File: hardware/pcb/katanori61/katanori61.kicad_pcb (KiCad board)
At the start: 2 copper layers, 82 x 37.4 mm, 59 parts, among them J1 XIAO RISER, J10 BAT (JST-PH), J13 USB-C, J2 OLED, J4 SPK IN, J5 SPK OUT, J6 BTN2, J7 REED+TOGGLE, K31 G6S-2F DC5, Q1 MMUN2133LT1G, Q2 AO3401A, Q31 SS8050, U1 TPS61090RSAR, U2 MCP73871-2CCI/ML, U3 INA226AIDGSR, U4 AS5600-ASOM

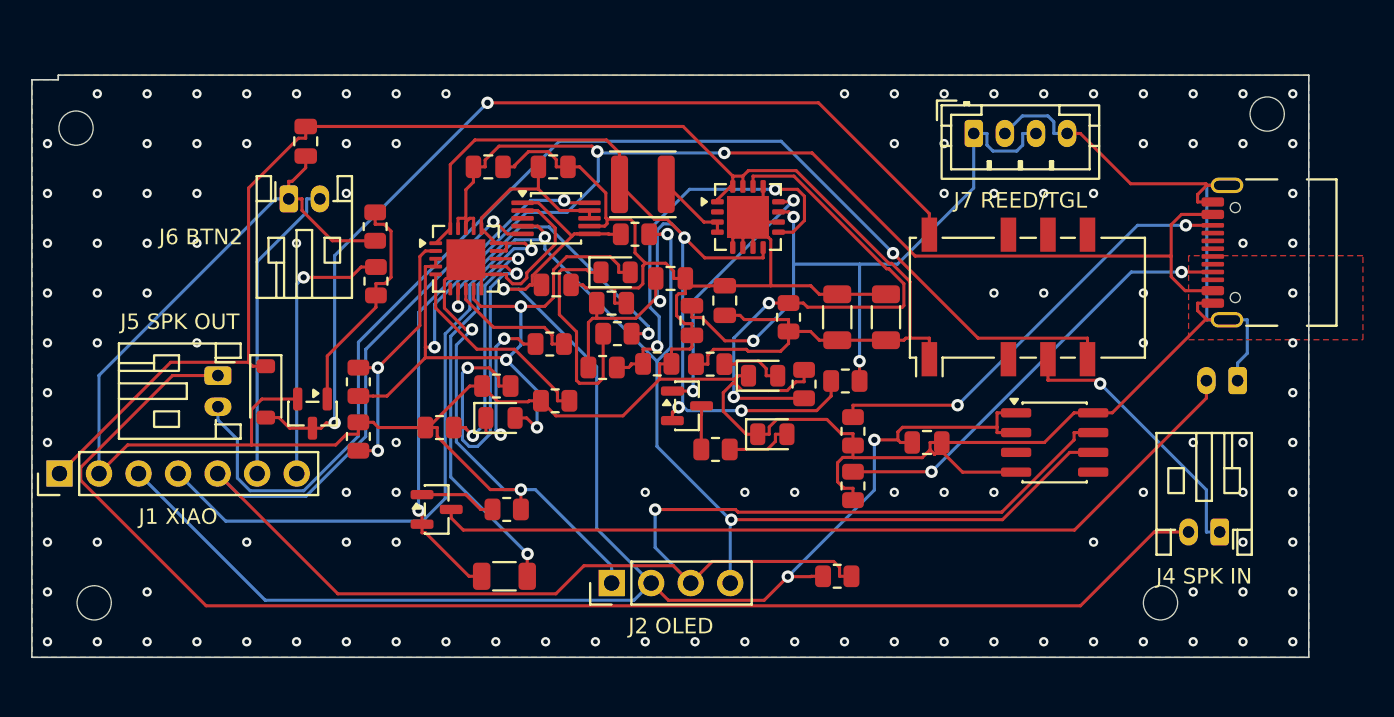
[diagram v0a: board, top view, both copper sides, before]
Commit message: pcb v6.1: J4 と J6 を縦の B2B-PH-K へ・J10 の極性を「手前が ＋ ・奥が GND」に戻す
🔒 ユーザー 2026-09-16 夕「J4とJ6を縦にして、J10の極性も手前奥に戻して」。

■ なぜ縦にしたか
J4（SPK IN）と J6（BTN2）は横出しで、抜く向きが**盤面の内側**（J4 は +Y・J6 は −Y）だった。
挿したプラグの胴が板の上へ 2.0 出るので、J4 は板の Y 14.30〜16.30、J6 は Y 21.20〜22.70 を塞ぐ。
gen_pcb の警告でも J4 の指の所に J13、J6 の指の所に R6・R7・D31・Q31・J1（背 8.5）が居て、
さらに「J6 の通り道が電池の下（挿し直すには電池を外す）」が出ていた。縦にすると全部消える。
筐体側は 56 個の模型でも plugpath が空で、殻は邪魔していない（別セッションが確認済み）。

■ J10 の極性が戻った
J10 のパッドを X 並びにしていたのは、J4 に挿さったプラグ（Y 14.30〜16.30）と
USB-C のシェルの足（20.63〜）に挟まれて 4.33 しか無く、6.9 の枠が入らなかったため。
J4 が縦になってその帯が消えたので **Y 並びへ戻した**。
  1 番 GND  → 板 (75.700, 16.950) ＝ 奥（ハッチ側）
  2 番 VBAT ＋ → 板 (75.700, 14.950) ＝ 手前（OLED 側）
PowerBoost B1 と同じ言い方に戻ったので、2026-09-16 夕に「左／右」で書き直した手順は
もう一度「手前／奥」に戻る。docs/PCB-V61.md 8 章を直した。

■ 置き直した枠（板の座標）
  J4  X 71.850〜78.750 / Y  6.250〜11.750（旧 Y 6.20〜14.80）。パッドは Y 8.45
      ⚠ 芯の Y は 9.00。8.60 だと枠の前端が取付穴 (72.5, 3.5) のナット（半径 2.56）へ 0.21 入る
  J6  X 14.050〜20.950 / Y 27.250〜32.750（旧 Y 22.70〜31.30）
  J10 X 73.500〜79.000 / Y 12.500〜19.400（旧 X 73.00〜79.90 / Y 14.475〜19.975）
      足は J4 の胴（Y 〜11.75）から 2.6・枠は USB-C の足（20.63）から 1.23

■ 足形は回路図が持っている
gen_pcb.py の BOX_PLACE だけ替えても足形は変わらない（place_footprint はネットリストの fp を使う）。
gen_sch.py の FP_PORT["PHIN"] と J6 の part() も B2B-PH-K へ替えること。
SPK OUT（J5）は口が板の**左の縁**（−X）を向いていて盤面を食わないので横出しのまま。
板の面に沿ってプラグが入るのは J5 だけになったので、gen_pcb の CONN も J5 だけにした。

■ 検査
回路図 0 件 / パッドの位置 11 点一致 / 重なり 0 / プラグの通り道 1 口すべて空き
DRC エラー 0・未接続 0・回路図との食い違い 0 / 銅箔のすきま 下回り 0 件（最小 0.151）
check_fab「奥（Y 16.95）が GND ／ 手前（Y 14.95）が VBAT」/ 地図の重なり なし
筐体 16 項目すべて期待値（hit_wires は 2.75 → 2.74）
STL 7 点 preflight: 中身 1 個・二重面 0・**🔴 0**（蓋の 0.22mm は 9072479 で解消済み）

■ 筐体側
pcb/v61_parts.scad を作り直した（gen_case_parts.py の PORTS も J4・J6 を上向きへ）。
SPK IN の線は「横から寄せて上から降ろす」形に引き直し。走る高さを
「嵌合したプラグの頭の 2.0 上」にした（旧 zl は横出しの背 4.8 を足した数で、縦の胴 6.0 ＋ 嵌合 2.0 より低く、プラグの頭を貫く）。
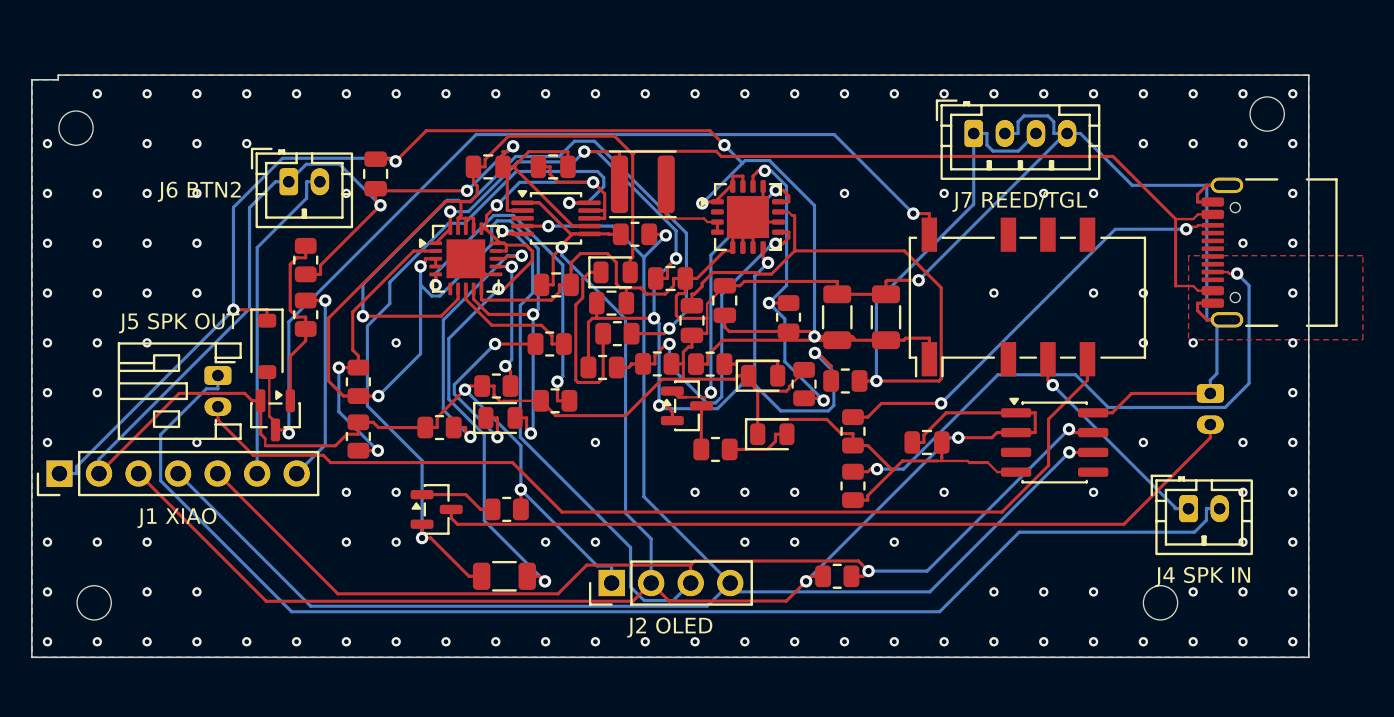
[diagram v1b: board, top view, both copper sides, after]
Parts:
- J4, J6: footprint Connector_JST:JST_PH_S2B-PH-K_1x02_P2.00mm_Horizontal -> Connector_JST:JST_PH_B2B-PH-K_1x02_P2.00mm_Vertical
- moved R31 5.00 mm to (57.6, 55.4)
- moved C31 4.96 mm to (62.1, 46.4)
- moved R32 4.95 mm to (57.6, 51.9)
- moved D31 2.93 mm to (55.1, 57.4)
- moved J4 2.50 mm to (114.3, 67.8), turned to 0 degrees
- moved Q31 2.38 mm to (55.6, 61.9)
- moved J10 1.93 mm to (115.7, 60.5), turned to 270 degrees
- moved J6 1.10 mm to (56.5, 46.9)
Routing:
- net STAT2: track 20.3 -> 45.5 mm
- net PROG3: track 23.6 -> 8.98 mm
- net SPKO: track 79.5 -> 65.8 mm, vias 1 -> 0
- net SCL: track 113.8 -> 100.2 mm, vias 2 -> 3
- net FB: track 35.0 -> 21.6 mm, vias 2 -> 3
- net BATP: track 33.3 -> 45.6 mm
- net EN: track 45.9 -> 57.5 mm, vias 3 -> 1
- net CC1: track 28.4 -> 38.5 mm
- net VBUS: track 125.7 -> 134.6 mm, vias 6 -> 4
- net THERM: track 13.5 -> 22.1 mm, vias 0 -> 2
- net VLIPO: track 41.8 -> 50.1 mm, vias 2 -> 4
- net V5: track 106.3 -> 113.8 mm, vias 0 -> 5
- net VSYS: track 71.9 -> 77.3 mm, vias 4 -> 7
- net SPKM: track 88.6 -> 83.4 mm
- net IN: track 17.7 -> 13.1 mm
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
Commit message: pcb v6.1: 前右の留め穴を外へ（板の X 72.5 → 79.354）。筐体 97fdee3 への追従
🔒 ユーザー「組む順で問題にならないのなら外側に出せるでしょ？」。筐体側が前右の柱を
世界 (74.5, 17) → (81.354, 17) へ出したので、板の穴も合わせる。

取付穴 4 点（板の座標）:
  左前 (4.0, 3.5)          左後ろ (2.834, 33.9942)
  右前 (79.354, 3.5) ←変更  右後ろ (79.354, 34.9)
右は前後とも X 79.354 でそろった。72.5 は「φ7 の柱の外周 78.0 が箱の隅の柱 78.354 まで 0.35」で
決まった数字で、後ろ 2 点を柱の芯へ出した e3a7162 のときに前右だけ内側に残っていた。

■ 検査
gen_pcb: パッドの位置 11 点一致・重なり 0・ナットの下に部品なし・パッドと穴のすきま 0.3 以上
DRC エラー 0・未接続 0・回路図との食い違い 0（自動配線は 1 回で 0 本残し）
check_pcb: 下回り 0 件（最小 0.151 = BATP ↔ VLIPO）
check_fab: 合わない所なし。取付穴 4 点とも φ2.20 を確認
地図の重なり なし

■ 筐体へ渡す物も作り直した
  v61_parts.scad   … 差分なし（穴は PCB_PARTS に入らない。部品も動いていない）
  v61_board3d.stl  … 板のメッシュ（穴が動いたので変わる）
  v61_parts3d.stl  … 差分なし
筐体の当たり検査 16 項目は穴を動かす前と全部同じ値で、STL 7 点も
中身 1 個・二重面 0・🔴 0 のまま（形は不変）。

⚠ 筐体側の指摘の記録: 「外へ出すと PH2（J4・J10）に当たる」は平面だけを見た誤りだった。
   柱は床から板の裏（Z 0〜12.0）、PH2 は板の上。Z では当たらない。
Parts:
- moved ? 6.85 mm to (119.4, 73.9)
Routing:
- net GND: vias 135 -> 136
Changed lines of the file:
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@@
 	(footprint "MountingHole:MountingHole_2.2mm_M2"
 		(layer "F.Cu")
-		(at 112.500 73.900)
+		(at 119.354 73.900)
 		(attr exclude_from_bom)
 		(pad "" np_thru_hole circle
@@
 	(segment
 		(start 66.9375 68.4517)
-		(end 67.3394 68.8536)
+		(end 67.3919 68.9061)
 		(width 0.200)
 		(layer "F.Cu")
@@
 	)
 	(segment
-		(start 67.3394 68.8536)
-		(end 110.1481 68.8536)
+		(start 67.3919 68.9061)
+		(end 110.0956 68.9061)
 		(width 0.200)
 		(layer "F.Cu")
@@
 	)
 	(segment
-		(start 110.1481 68.8536)
+		(start 110.0956 68.9061)
 		(end 115.7000 63.3017)
 		(width 0.200)
@@
 	(segment
 		(start 48.2681 66.0546)
-		(end 56.6872 74.4737)
+		(end 56.7364 74.5229)
 		(width 0.200)
 		(layer "B.Cu")
@@
 	)
 	(segment
-		(start 56.6872 74.4737)
-		(end 98.3110 74.4737)
+		(start 56.7364 74.5229)
+		(end 109.5206 74.5229)
 		(width 0.200)
 		(layer "B.Cu")
@@
 	)
 	(segment
-		(start 98.3110 74.4737)
-		(end 103.4220 69.3627)
-		(width 0.200)
-		(layer "B.Cu")
-		(net 24)
-	)
-	(segment
-		(start 103.4220 69.3627)
-		(end 114.6808 69.3627)
-		(width 0.200)
-		(layer "B.Cu")
-		(net 24)
-	)
-	(segment
-		(start 114.6808 69.3627)
+		(start 109.5206 74.5229)
 		(end 115.4483 68.5952)
 		(width 0.200)
@@
 	)
 	(via
+		(at 105.0000 70.0000)
+		(size 0.6)
+		(drill 0.3)
+		(layers "F.Cu" "B.Cu")
+		(net 11)
+	)
+	(via
 		(at 105.0000 47.6000)
 		(size 0.6)
@@
 	)
 	(via
+		(at 108.2000 70.0000)
+		(size 0.6)
+		(drill 0.3)
+		(layers "F.Cu" "B.Cu")
+		(net 11)
+	)
+	(via
 		(at 108.2000 66.8000)
 		(size 0.6)
@@
 	)
 	(via
+		(at 111.4000 70.0000)
+		(size 0.6)
+		(drill 0.3)
+		(layers "F.Cu" "B.Cu")
+		(net 11)
+	)
+	(via
 		(at 111.4000 63.6000)
 		(size 0.6)
@@
 	)
 	(via
-		(at 117.8000 73.2000)
-		(size 0.6)
-		(drill 0.3)
-		(layers "F.Cu" "B.Cu")
-		(net 11)
-	)
-	(via
 		(at 117.8000 70.0000)
 		(size 0.6)
@@
 		(size 0.6)
 		(drill 0.3)
-		(layers "F.Cu" "B.Cu")
-		(net 11)
-	)
-	(via
-		(at 121.0000 73.2000)
-		(size 0.6)
-		(drill 0.3)

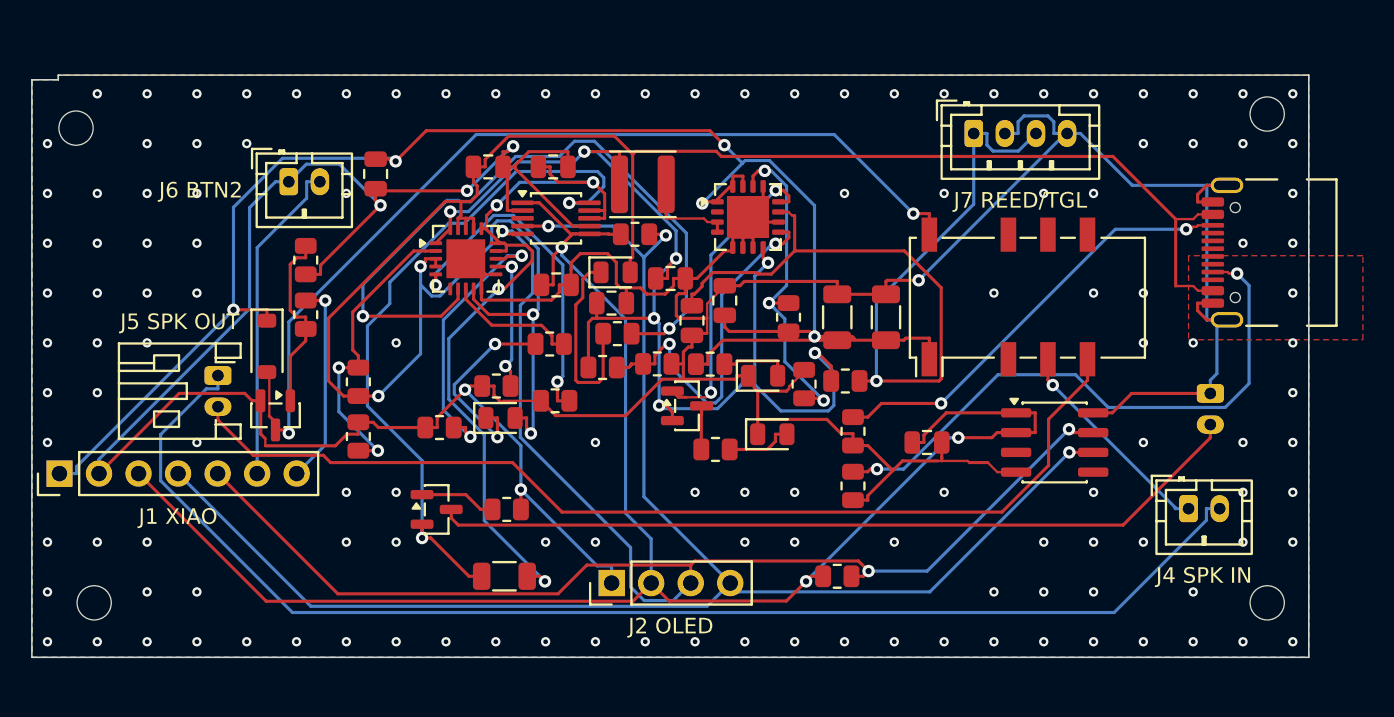
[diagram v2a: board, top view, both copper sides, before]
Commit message: pcb v6.1: 電源部を電流の順に並べ直す（電池の道 217 → 11.4 mΩ・INA226 のケルビン成立）
電源部は旧 PowerBoost 基板 → v6 → v6.1 の**二重の写し**で置かれていて、
v6.1 の板の上で並べた人がいなかった（gen_pcb.py の写しの注「ここで並べ直して
はいない」のまま）。その結果:

  ・電池の口 J10（板 X 76）からシャント R41（X 30）まで電流が板を横断し、
    自動配線の既定 0.2mm のままで配線 107mm ＝ 217mΩ
  ・シャント R41 と電流計 U3 が 23mm 離れ、センス線が R41 のパッドではなく
    11.9mΩ 手前（Q2 の足元）と 73.7mΩ 先（U2 の VBAT）から出ていた。
    INA226 は 10mΩ ではなく 96.7mΩ ＝ **9.7 倍**を見ていた
  ・USB-C J13 から充電 IC U2 まで 52mm

v5 で正しく読めていたのは、INA226 モジュールの上でシャントと IC が数 mm しか
離れておらず、ケルビンがモジュールの中で取れていたからである。v6.1 でシャントを
板に降ろしたときに、回路図（同じネット）は写ったが置き方（同じ点）が写らなかった。

並べ直し（板の座標で明示・写しをやめた）:
  J10 電池 → Q2 逆接保護 → R41 シャント → U2 充電 → L1・U1 昇圧 → J1 XIAO
  U3 は R41 の真上。USB-C は U2 のすぐ前の縁へ。

  電池の道      107mm 217.2mΩ → 13.7mm 11.4mΩ（充電 560mA で 6.4mV・1A で 11.4mV）
  R41 → U3      23.2mm → 3.0mm
  J13 → U2      52.0mm → 12.9mm
  ホットループ  7.4mm → 3.3mm（U1 を 180° 回して SW を L1 の側へ）
  SW            6.2mm → 4.6mm

入れた仕組み:
  ・dsn.py    ネットの組ごとの線幅（電池 0.6 / VSYS・SW・V5 0.4 / VBUS 0.2）
  ・gen_pcb.py PRE_TRACKS … 先に手で引いて固定する線。R41 のケルビン 2 本。
               ep_vias()  … U1・U2 の放熱パッドに GND ビア 4 本ずつ（配置から計算）
  ・route.py  locked の線と穴を merge で残し、SES に返る protect の写しは捨てる
  ・gen_sch.py R41 に「ケルビン必須・PRE_TRACKS を見よ」と経緯ごと残した

ついでに直したもの:
  ・USB-C を動かしたのに VBUS のベタが板の右端に残っていた（isolated_copper）。
    口の向きに追従させた
  ・Freerouting の最適化の段が、配線の段より悪い版から始めて書き出す（未接続 1 → 6）。
    統合基板で 2026-09-15 に見たのと同じ不具合。v6.1 側でも切った

検算: 未接続 0 ／ 回路図との差 0 ／ DRC エラー 0 ／ 銅のすきま 下回り 0。
ケルビンは「負荷の道 ＋ センス線 ＝ 直に測った値」の一致で成立を確認した。

残る警告: silk_over_copper 2 件（U1・U2 のシルクの角が隣のパッドに 0.1 乗る。
逃がすと未接続が 2 本出たので警告を取った）。lib_footprint_issues 59 件と
silk_edge_clearance 2 件は以前からあるもの。
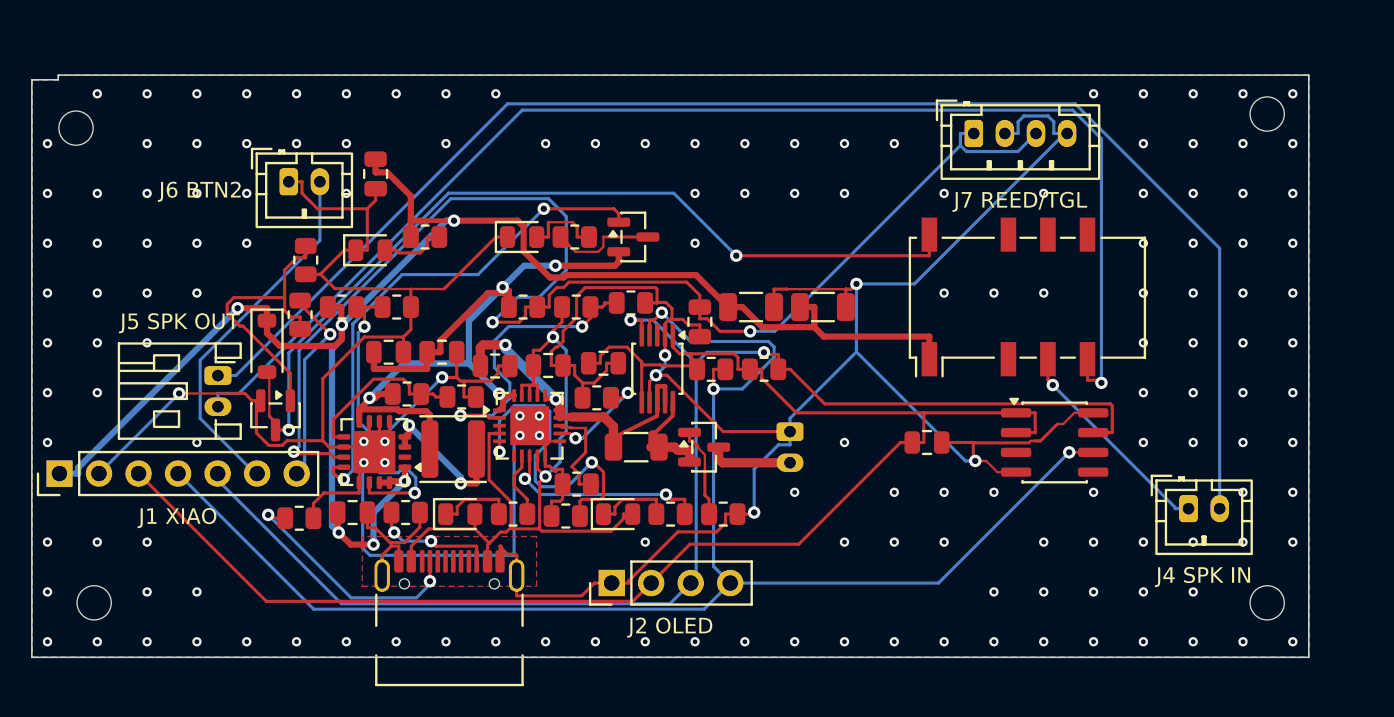
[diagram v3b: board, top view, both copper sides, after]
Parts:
- removed the C31 at (62.1, 46.4)
- removed the D31 at (55.1, 57.4)
- removed the R31 at (57.6, 55.4)
- removed the R32 at (57.6, 51.9)
- removed the R5 at (83.6, 58.6)
- added C7: 10uF, Capacitor_SMD:C_0805_2012Metric, F.Cu at (69.8, 58.7)
- added C8: 10uF, Capacitor_SMD:C_0805_2012Metric, F.Cu at (73.2, 58.7)
- added R44: 5.1k, Resistor_SMD:R_0805_2012Metric, F.Cu at (57.2, 68.5)
- added R45: 5.1k, Resistor_SMD:R_0805_2012Metric, F.Cu at (64.0, 68.1)
- added R46: 100K, Resistor_SMD:R_0805_2012Metric, F.Cu at (84.4, 68.2)
- C31: renamed from R44; value 5.1k -> 0.1uF; footprint Resistor_SMD:R_0805_2012Metric -> Capacitor_SMD:C_0805_2012Metric
- D31: renamed from C7; value 10uF -> 1N4148W; footprint Capacitor_SMD:C_0805_2012Metric -> Diode_SMD:D_SOD-123
- R31: renamed from C8; value 10uF -> 1k; footprint Capacitor_SMD:C_0805_2012Metric -> Resistor_SMD:R_0805_2012Metric
- R32: renamed from R45; value 5.1k -> 10k
- R5: renamed from R46; value 100K -> 1K
- moved J13 58.2 mm to (66.8, 75.3), turned to 0 degrees
- moved R32 36.8 mm to (57.6, 51.9)
- moved C31 36.6 mm to (62.1, 46.4)
- moved R3 28.7 mm to (59.9, 54.9), turned to 0 degrees
- moved U1 28.4 mm to (62.0, 64.2), turned to 180 degrees
- moved C2 27.5 mm to (60.6, 68.1), turned to 0 degrees
- moved J10 27.1 mm to (88.7, 62.9)
- moved R4 26.6 mm to (63.4, 54.9), turned to 0 degrees
- moved LED2 26.5 mm to (61.7, 51.2)
- moved D31 21.7 mm to (55.1, 57.4), turned to 270 degrees
- moved R13 21.2 mm to (71.6, 54.9)
- moved L1 20.9 mm to (67.1, 64.0)
- moved LED1 20.5 mm to (71.5, 50.4)
- moved R7 19.5 mm to (78.5, 54.6), turned to 0 degrees
- moved LED3 18.5 mm to (67.5, 68.2)
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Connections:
- C31 pad 1: CC1 -> V5
- D31 pad 1: VLIPO -> V5
- D31 pad 2: GND -> COL
- R31 pad 1: VBUS -> IN
- R31 pad 2: GND -> BASE
- R32 pad 1: CC2 -> BASE
- R5 pad 1: BATG -> V5
- R5 pad 2: GND -> N_LED2
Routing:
- net VBUS: track 134.6 -> 51.1 mm, vias 4 -> 2
- net BATRAW: track 52.7 -> 5.44 mm
- net STAT2: track 45.5 -> 4.30 mm, vias 2 -> 0
- net BATP: track 45.6 -> 6.78 mm, vias 2 -> 0
- net EN: track 57.5 -> 87.4 mm, vias 1 -> 3
- net VLIPO: track 50.1 -> 21.1 mm, vias 4 -> 2
- net VSYS: track 77.3 -> 51.3 mm, vias 7 -> 4
- net CC1: track 38.5 -> 15.6 mm
- net CC2: track 28.2 -> 7.99 mm
- net SPKO: track 65.8 -> 83.9 mm, vias 0 -> 1
- net LBO: track 19.5 -> 32.9 mm
- net GND: track 293.5 -> 280.5 mm, vias 136 -> 159
- net V33: track 113.5 -> 100.7 mm, vias 3 -> 0
- net LBI: track 23.7 -> 11.0 mm, vias 2 -> 0
- net SCL: track 100.2 -> 87.9 mm, vias 3 -> 2
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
